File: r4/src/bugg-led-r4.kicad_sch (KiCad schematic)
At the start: 22 parts, among them J201 2314844-8, J202 FH12A-20S-0.5SH

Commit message: Update footprints. Fix missing soldermask cutouts in mounting holes
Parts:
- H201, H202, H203, H204: footprint MountingHole:MountingHole_3.2mm_M3_DIN965 -> jeffmakes-footprints:MountingHole_3.2mm_M3_DIN965_no_soldermask
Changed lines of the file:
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@@
       (effects (font (size 1.27 1.27)) (justify left))
     )
-    (property "Footprint" "MountingHole:MountingHole_3.2mm_M3_DIN965" (at 114.3 30.48 0)
+    (property "Footprint" "jeffmakes-footprints:MountingHole_3.2mm_M3_DIN965_no_soldermask" (at 114.3 30.48 0)
       (effects (font (size 1.27 1.27)) hide)
     )
@@
       (project "bugg-led-r4"
         (path "/79d27b01-4301-4e81-9656-f37ccd19516d"
-          (reference "H201") (unit 1) (value "MountingHole_3.2mm_M3_DIN965") (footprint "MountingHole:MountingHole_3.2mm_M3_DIN965")
+          (reference "H201") (unit 1) (value "MountingHole_3.2mm_M3_DIN965") (footprint "jeffmakes-footprints:MountingHole_3.2mm_M3_DIN965_no_soldermask")
         )
       )
@@
       (effects (font (size 1.27 1.27)) (justify left))
     )
-    (property "Footprint" "MountingHole:MountingHole_3.2mm_M3_DIN965" (at 114.3 36.83 0)
+    (property "Footprint" "jeffmakes-footprints:MountingHole_3.2mm_M3_DIN965_no_soldermask" (at 114.3 36.83 0)
       (effects (font (size 1.27 1.27)) hide)
     )
@@
       (project "bugg-led-r4"
         (path "/79d27b01-4301-4e81-9656-f37ccd19516d"
-          (reference "H202") (unit 1) (value "MountingHole_3.2mm_M3_DIN965") (footprint "MountingHole:MountingHole_3.2mm_M3_DIN965")
+          (reference "H202") (unit 1) (value "MountingHole_3.2mm_M3_DIN965") (footprint "jeffmakes-footprints:MountingHole_3.2mm_M3_DIN965_no_soldermask")
         )
       )
@@
       (effects (font (size 1.27 1.27)) (justify left))
     )
-    (property "Footprint" "MountingHole:MountingHole_3.2mm_M3_DIN965" (at 114.3 49.53 0)
+    (property "Footprint" "jeffmakes-footprints:MountingHole_3.2mm_M3_DIN965_no_soldermask" (at 114.3 49.53 0)
       (effects (font (size 1.27 1.27)) hide)
     )
@@
       (project "bugg-led-r4"
         (path "/79d27b01-4301-4e81-9656-f37ccd19516d"
-          (reference "H204") (unit 1) (value "MountingHole_3.2mm_M3_DIN965") (footprint "MountingHole:MountingHole_3.2mm_M3_DIN965")
+          (reference "H204") (unit 1) (value "MountingHole_3.2mm_M3_DIN965") (footprint "jeffmakes-footprints:MountingHole_3.2mm_M3_DIN965_no_soldermask")
         )
       )
@@
       (effects (font (size 1.27 1.27)) (justify left))
     )
-    (property "Footprint" "MountingHole:MountingHole_3.2mm_M3_DIN965" (at 114.3 43.18 0)
+    (property "Footprint" "jeffmakes-footprints:MountingHole_3.2mm_M3_DIN965_no_soldermask" (at 114.3 43.18 0)
       (effects (font (size 1.27 1.27)) hide)
     )
@@
       (project "bugg-led-r4"
         (path "/79d27b01-4301-4e81-9656-f37ccd19516d"
-          (reference "H203") (unit 1) (value "MountingHole_3.2mm_M3_DIN965") (footprint "MountingHole:MountingHole_3.2mm_M3_DIN965")
-        )
-      )
+          (reference "H203") (unit 1) (value "MountingHole_3.2mm_M3_DIN965") (footprint "jeffmakes-footprints:MountingHole_3.2mm_M3_DIN965_no_soldermask")
+        )
+      )

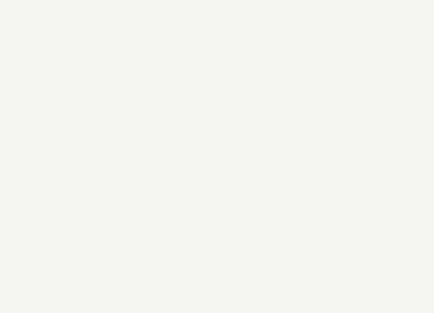
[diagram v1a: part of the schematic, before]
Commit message: Change submodule settings so, hopefully, submodules don't get into a detatched-head state (https://stackoverflow.com/questions/7124486/what-to-do-with-commit-made-in-a-detached-head)
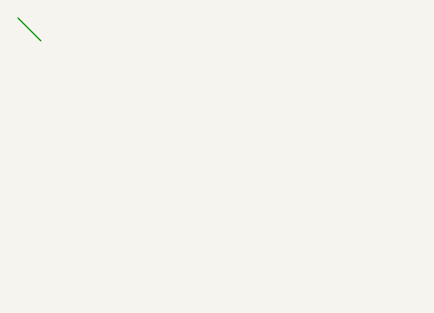
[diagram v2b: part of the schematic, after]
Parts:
- H205, H206: footprint (none) -> jeffmakes-footprints:MountingHole_2.0mm
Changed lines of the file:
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@@
   (junction (at 185.42 72.39) (diameter 1.016) (color 0 0 0 0)
+  )
+  (bus_entry (at 40.64 21.59) (size 2.54 2.54)
+    (stroke (width 0) (type default))
   )
   (wire (pts (xy 119.38 124.46) (xy 124.46 124.46))
@@
       (effects (font (size 1.27 1.27)) (justify left))
     )
-    (property "Footprint" "" (at 165.1 36.83 0)
+    (property "Footprint" "jeffmakes-footprints:MountingHole_2.0mm" (at 165.1 36.83 0)
       (effects (font (size 1.27 1.27)) hide)
     )
@@
       (project "bugg-led-r4"
         (path "/79d27b01-4301-4e81-9656-f37ccd19516d"
-          (reference "H206") (unit 1) (value "MountingHole") (footprint "")
+          (reference "H206") (unit 1) (value "MountingHole") (footprint "jeffmakes-footprints:MountingHole_2.0mm")
         )
       )
@@
       (effects (font (size 1.27 1.27)) (justify left))
     )
-    (property "Footprint" "" (at 165.1 30.48 0)
+    (property "Footprint" "jeffmakes-footprints:MountingHole_2.0mm" (at 165.1 30.48 0)
       (effects (font (size 1.27 1.27)) hide)
     )
@@
       (project "bugg-led-r4"
         (path "/79d27b01-4301-4e81-9656-f37ccd19516d"
-          (reference "H205") (unit 1) (value "MountingHole") (footprint "")
-        )
-      )
+          (reference "H205") (unit 1) (value "MountingHole") (footprint "jeffmakes-footprints:MountingHole_2.0mm")
+        )
+      )
